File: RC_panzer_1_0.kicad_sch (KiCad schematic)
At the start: 13 parts, among them J1 Conn_01x19_Socket, J10 StepDown_OUT, J2 Conn_01x19_Socket, J3 Motortreiber_links, J4 Motortreiber_rechts, J5 Stepper_driver_links, J6 Stepper_driver_rechts, J7 Screw_Terminal_01x02, J8 Stepper_Ausgang, J9 StepDown_IN

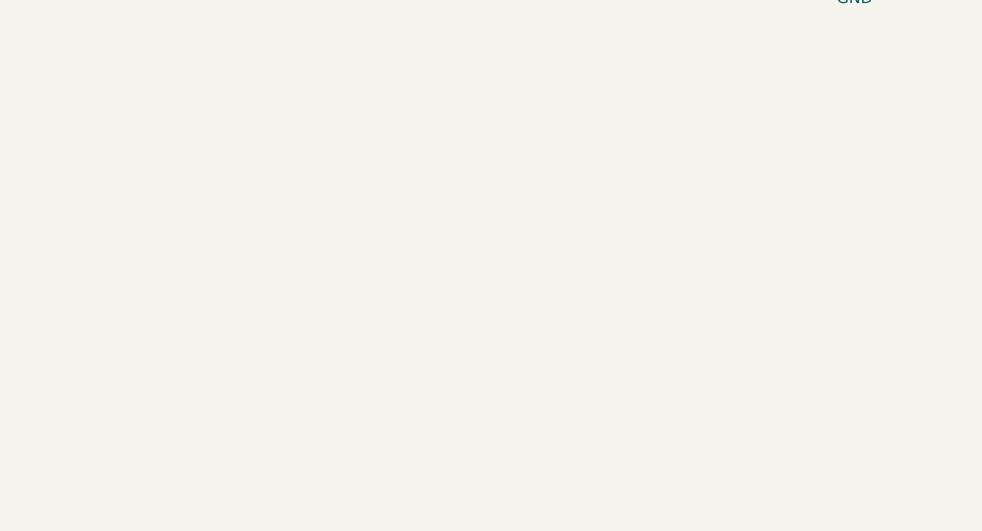
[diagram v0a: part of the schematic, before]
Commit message: including TB6612 as h -brige / motor driver bc old drivers where to big and stupid
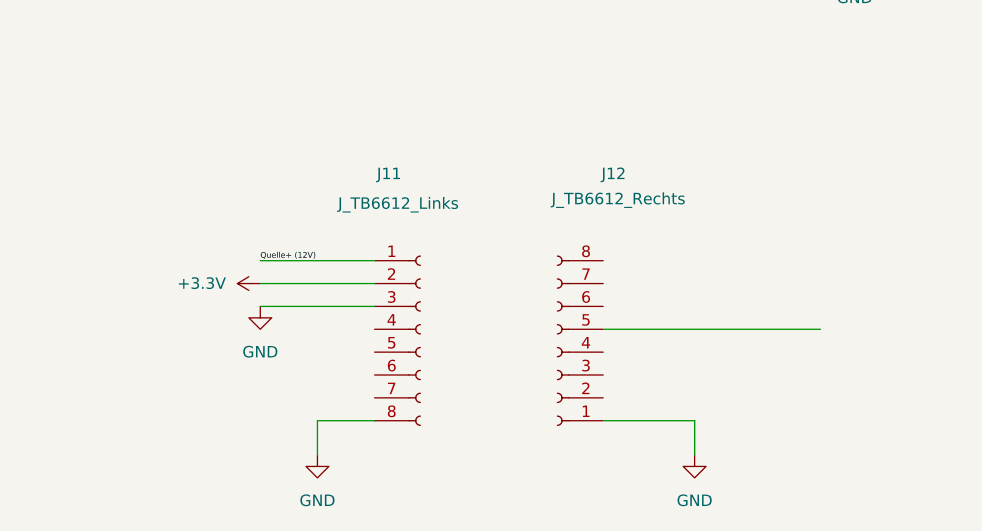
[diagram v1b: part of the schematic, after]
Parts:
- added J11: J_TB6612_Links, symbol Connector:Conn_01x08_Socket
- added J12: J_TB6612_Rechts, symbol Connector:Conn_01x08_Socket
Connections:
- net +3.3V: now also J11.2 (Pin_2)
- net GND: now also J11.3 (Pin_3), J11.8 (Pin_8), J12.1 (Pin_1)
- net Quelle+ (12V): now also J11.1 (Pin_1)

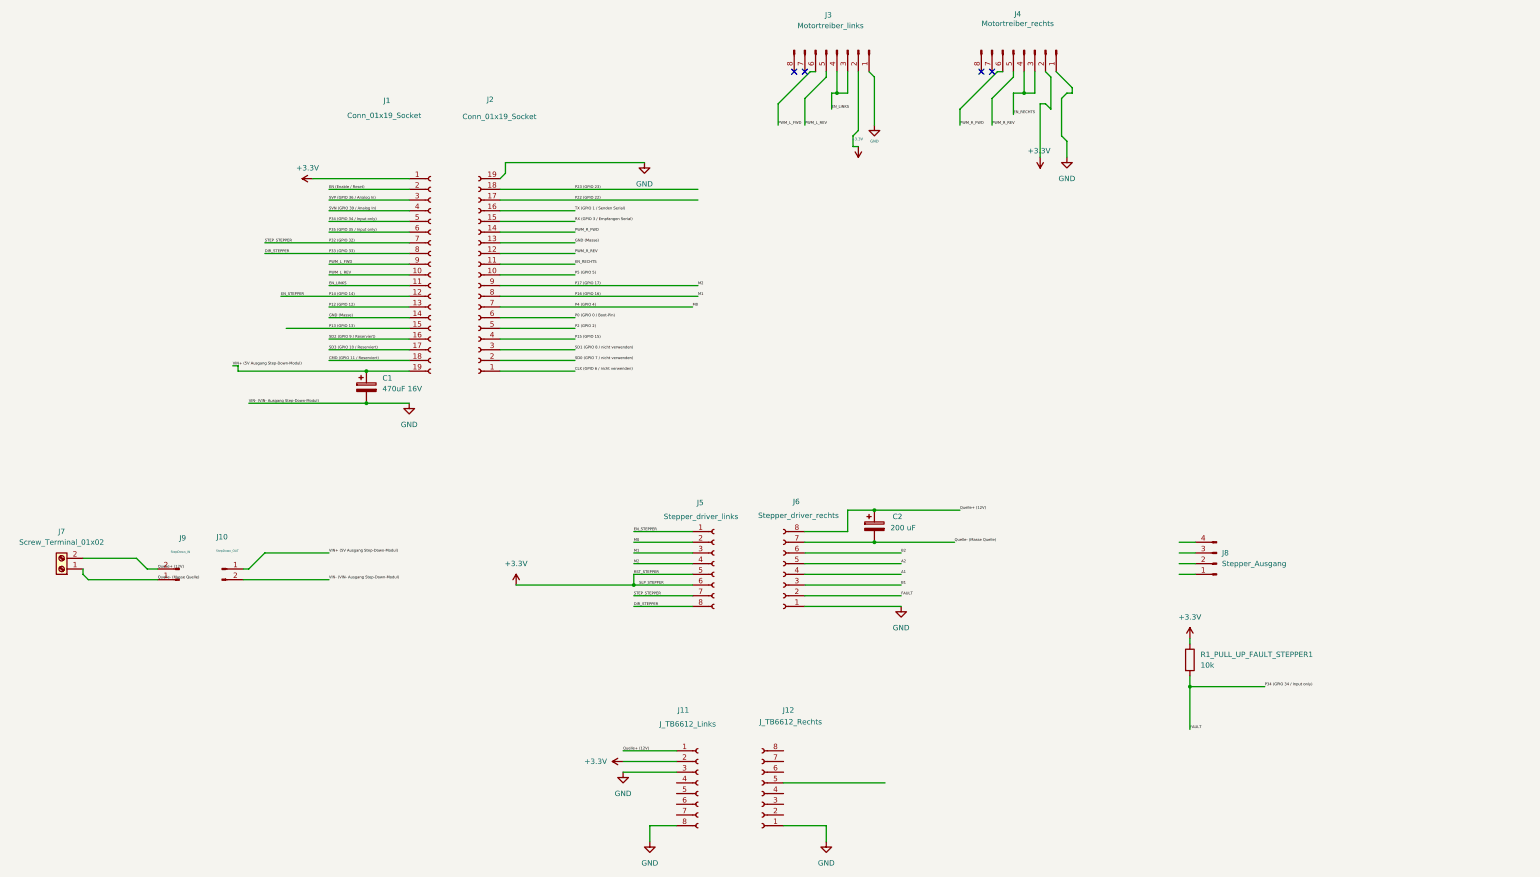
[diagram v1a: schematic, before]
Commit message: working on h-brige that it continues
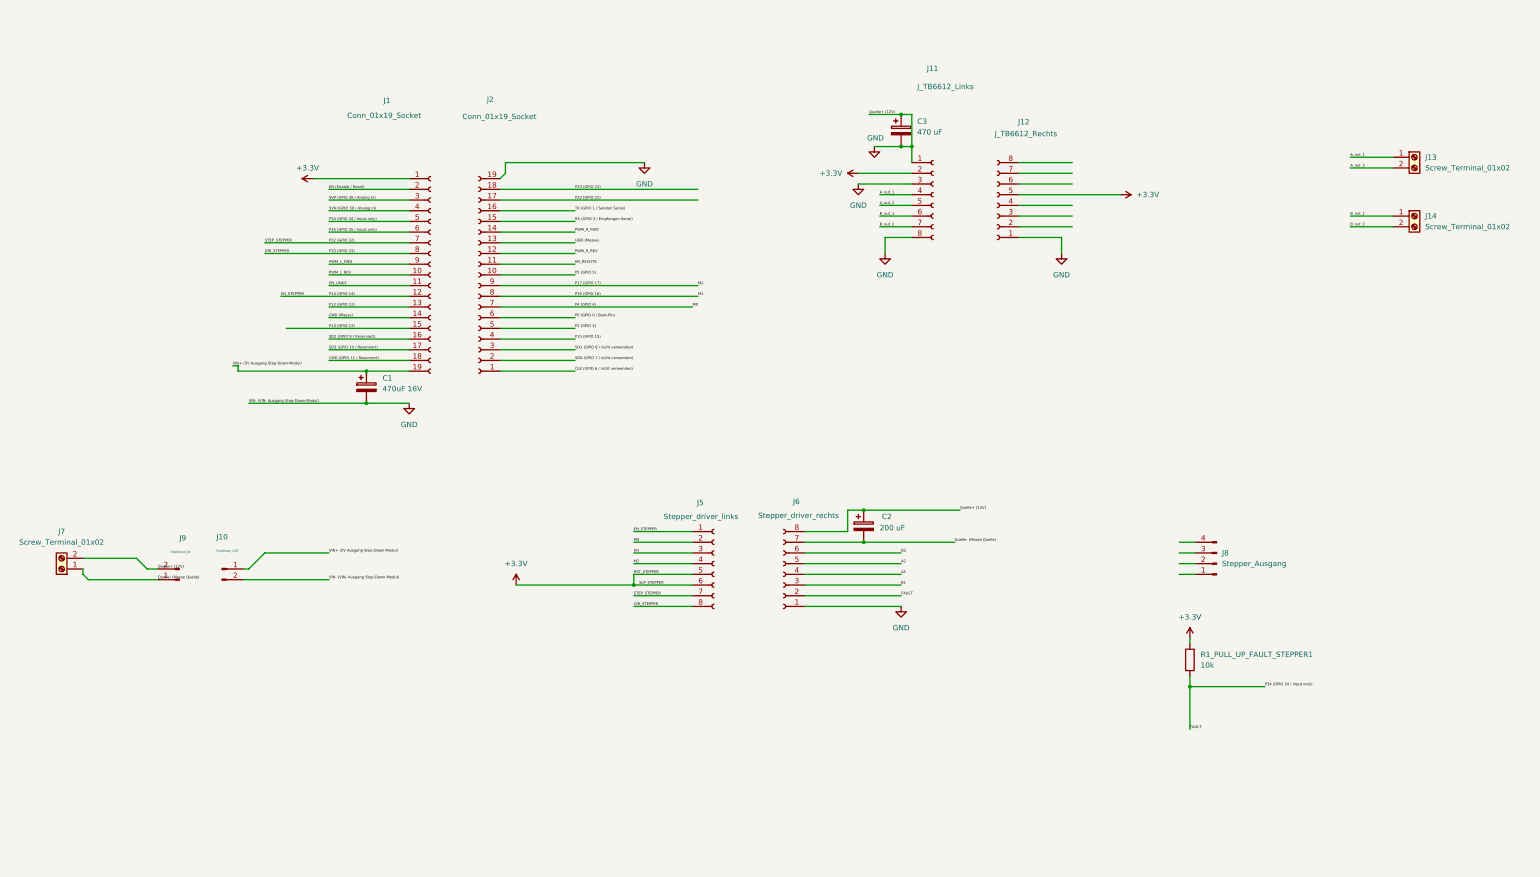
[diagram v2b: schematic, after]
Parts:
- removed J3: Motortreiber_links, Connector_PinHeader_2.54mm:PinHeader_1x08_P2.54mm_Vertical, symbol Connector:Conn_01x08_Pin
- removed J4: Motortreiber_rechts, Connector_PinHeader_2.54mm:PinHeader_1x08_P2.54mm_Vertical, symbol Connector:Conn_01x08_Pin
- added C3: 470 uF, Capacitor_THT:CP_Radial_D10.0mm_P5.00mm, symbol Device:C_Polarized
- added J13, J14: Screw_Terminal_01x02, TerminalBlock_Phoenix:TerminalBlock_Phoenix_MKDS-1,5-2_1x02_P5.00mm_Horizontal, symbol Connector:Screw_Terminal_01x02
- J11, J12: footprint (none) -> Connector_PinSocket_2.54mm:PinSocket_1x08_P2.54mm_Vertical
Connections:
- net Quelle+ (12V) is gone; now on net GND: C2.1, J11.1 (Pin_1), J6.8 (Pin_8), J7.2 (Pin_2), J9.2 (Pin_2)
- net +3.3V: now also J12.5 (Pin_5)
- net GND: now also C3.1, C3.2
- net A_out_1: now reaches J11.4 (Pin_4)
- net A_out_1: now also J13.1 (Pin_1)
- net A_out_2: now reaches J11.5 (Pin_5)
- net A_out_2: now also J13.2 (Pin_2)
- net B_out_1: now reaches J11.6 (Pin_6)
- net B_out_1: now also J14.1 (Pin_1)
- net B_out_2: now reaches J11.7 (Pin_7)
- net B_out_2: now also J14.2 (Pin_2)
- no-connect marks 4 -> 0
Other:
- moved on the sheet: C2, J11, J12

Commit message: clearing somthings
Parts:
- C1: footprint Capacitor_THT:CP_Axial_L42.5mm_D20.0mm_P49.00mm_Horizontal -> Capacitor_THT:CP_Radial_D10.0mm_P3.50mm
- C2: footprint Capacitor_THT:CP_Axial_L42.0mm_D32.0mm_P45.00mm_Horizontal -> Capacitor_THT:CP_Radial_D8.0mm_P5.00mm
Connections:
- net Quelle- (Masse Quelle) is gone; now on net GND: C2.2, J6.7 (Pin_7), J7.1 (Pin_1), J9.1 (Pin_1)
- net GND: no longer C2.1, C3.1, J6.8 (Pin_8), J7.2 (Pin_2), J9.2 (Pin_2)
- new net Quelle+ (12V): C2.1, C3.1, J6.8 (Pin_8), J7.2 (Pin_2), J9.2 (Pin_2)
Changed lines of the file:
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@@
 	)
 	(junction
-		(at 96.52 110.49)
+		(at 46.99 160.02)
 		(diameter 0)
 		(color 0 0 0 0)
 	)
 	(junction
-		(at 226.06 57.15)
+		(at 96.52 110.49)
 		(diameter 0)
 		(color 0 0 0 0)
@@
 	)
 	(junction
-		(at 223.52 49.53)
-		(diameter 0)
-		(color 0 0 0 0)
-	)
-	(junction
 		(at 292.1 185.42)
 		(diameter 0)
@@
 	(wire
 		(pts
-			(xy 226.06 49.53) (xy 226.06 57.15)
-		)
-		(stroke
-			(width 0)
-			(type default)
-		)
-	)
-	(wire
-		(pts
 			(xy 330.2 76.2) (xy 340.36 76.2)
 		)
@@
 	(wire
 		(pts
+			(xy 46.99 160.02) (xy 46.99 168.91)
+		)
+		(stroke
+			(width 0)
+			(type default)
+		)
+	)
+	(wire
+		(pts
 			(xy 219.71 78.74) (xy 226.06 78.74)
 		)
@@
 	(wire
 		(pts
-			(xy 223.52 49.53) (xy 226.06 49.53)
+			(xy 213.36 66.04) (xy 226.06 66.04)
 		)
 		(stroke
@@
 	(wire
 		(pts
-			(xy 213.36 66.04) (xy 226.06 66.04)
+			(xy 83.82 64.77) (xy 106.68 64.77)
 		)
 		(stroke
@@
 	(wire
 		(pts
-			(xy 83.82 64.77) (xy 106.68 64.77)
+			(xy 128.27 67.31) (xy 175.26 67.31)
 		)
 		(stroke
@@
 	(wire
 		(pts
-			(xy 128.27 67.31) (xy 175.26 67.31)
+			(xy 96.52 118.11) (xy 106.68 118.11)
 		)
 		(stroke
@@
 	(wire
 		(pts
-			(xy 96.52 118.11) (xy 106.68 118.11)
+			(xy 129.54 60.96) (xy 129.54 63.5)
 		)
 		(stroke
@@
 	(wire
 		(pts
-			(xy 129.54 60.96) (xy 129.54 63.5)
+			(xy 77.47 100.33) (xy 106.68 100.33)
 		)
 		(stroke
@@
 	(wire
 		(pts
-			(xy 77.47 100.33) (xy 106.68 100.33)
+			(xy 45.72 170.18) (xy 46.99 168.91)
 		)
 		(stroke
@@
 		)
 	)
-	(label "Quelle- (Masse Quelle)"
-		(at 236.22 151.13 0)
-		(effects
-			(font
-				(size 0.635 0.635)
-			)
-			(justify left bottom)
-		)
-	)
 	(label "A1"
 		(at 223.52 158.75 0)
@@
 			)
 		)
-		(property "Footprint" "Capacitor_THT:CP_Axial_L42.5mm_D20.0mm_P49.00mm_Horizontal"
+		(property "Footprint" "Capacitor_THT:CP_Radial_D10.0mm_P3.50mm"
 			(at 97.4852 118.11 0)
 			(hide yes)
@@
 	)
 	(symbol
+		(lib_id "power:GND")
+		(at 236.22 151.13 0)
+		(unit 1)
+		(body_style 1)
+		(exclude_from_sim no)
+		(in_bom yes)
+		(on_board yes)
+		(in_pos_files yes)
+		(dnp no)
+		(fields_autoplaced yes)
+		(property "Reference" "#PWR05"
+			(at 236.22 157.48 0)
+			(hide yes)
+			(show_name no)
+			(do_not_autoplace no)
+			(effects
+				(font
+					(size 1.27 1.27)
+				)
+			)
+		)
+		(property "Value" "GND"
+			(at 236.22 156.21 0)
+			(show_name no)
+			(do_not_autoplace no)
+			(effects
+				(font
+					(size 1.27 1.27)
+				)
+			)
+		)
+		(property "Footprint" ""
+			(at 236.22 151.13 0)
+			(hide yes)
+			(show_name no)
+			(do_not_autoplace no)
+			(effects
+				(font
+					(size 1.27 1.27)
+				)
+			)
+		)
+		(property "Datasheet" ""
+			(at 236.22 151.13 0)
+			(hide yes)
+			(show_name no)
+			(do_not_autoplace no)
+			(effects
+				(font
+					(size 1.27 1.27)
+				)
+			)
+		)
+		(property "Description" "Power symbol creates a global label with name \"GND\" , ground"
+			(at 236.22 151.13 0)
+			(hide yes)
+			(show_name no)
+			(do_not_autoplace no)
+			(effects
+				(font
+					(size 1.27 1.27)
+				)
+			)
+		)
+		(pin "1"
+		)
+		(instances
+			(project "RC_panzer_1_0"
+				(path "/6c9e5231-ce36-4742-8ba3-3a3b16c58f9f"
+					(reference "#PWR05")
+					(unit 1)
+				)
+			)
+		)
+	)
+	(symbol
 		(lib_id "Connector:Screw_Terminal_01x02")
 		(at 345.44 73.66 0)
@@
 			)
 		)
-		(property "Footprint" "Capacitor_THT:CP_Axial_L42.0mm_D32.0mm_P45.00mm_Horizontal"
+		(property "Footprint" "Capacitor_THT:CP_Radial_D8.0mm_P5.00mm"
 			(at 215.5952 151.13 0)
 			(hide yes)
@@
 					(unit 1)
 				)
+			)
+		)
+	)
+	(symbol
+		(lib_id "power:GND")
+		(at 45.72 170.18 0)
+		(unit 1)
+		(body_style 1)
+		(exclude_from_sim no)
+		(in_bom yes)
+		(on_board yes)
+		(in_pos_files yes)
+		(dnp no)
+		(fields_autoplaced yes)
+		(property "Reference" "#PWR06"
+			(at 45.72 176.53 0)
+			(hide yes)
+			(show_name no)
+			(do_not_autoplace no)
+			(effects
+				(font
+					(size 1.27 1.27)
+				)
+			)
+		)
+		(property "Value" "GND"
+			(at 45.72 175.26 0)
+			(show_name no)
+			(do_not_autoplace no)
+			(effects
+				(font
+					(size 1.27 1.27)
+				)
+			)
+		)
+		(property "Footprint" ""
+			(at 45.72 170.18 0)
+			(hide yes)
+			(show_name no)
+			(do_not_autoplace no)
+			(effects
+				(font
+					(size 1.27 1.27)
+				)
+			)
+		)
+		(property "Datasheet" ""
+			(at 45.72 170.18 0)
+			(hide yes)
+			(show_name no)
+			(do_not_autoplace no)
+			(effects
+				(font
+					(size 1.27 1.27)
+				)
+			)
+		)
+		(property "Description" "Power symbol creates a global label with name \"GND\" , ground"
+			(at 45.72 170.18 0)
+			(hide yes)
+			(show_name no)
+			(do_not_autoplace no)
+			(effects
+				(font
+					(size 1.27 1.27)
+				)
+			)
+		)
+		(pin "1"
+		)
+		(instances
+			(project "RC_panzer_1_0"
+				(path "/6c9e5231-ce36-4742-8ba3-3a3b16c58f9f"
+					(reference "#PWR06")
+					(unit 1)
+				)
